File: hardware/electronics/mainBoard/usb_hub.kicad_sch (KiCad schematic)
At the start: 18 parts, among them J4 MUSBRM1C1M0, U4 USB2422-I/MJ

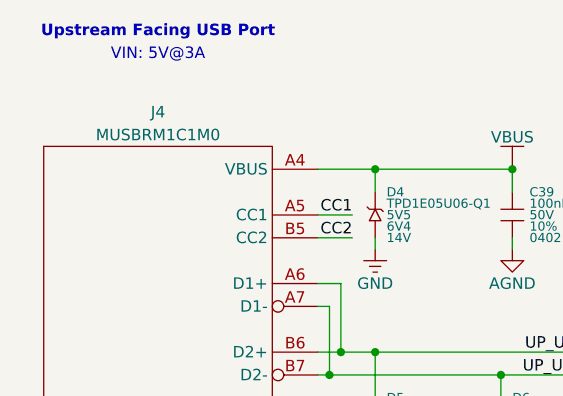
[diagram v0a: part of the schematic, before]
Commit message: renumber references
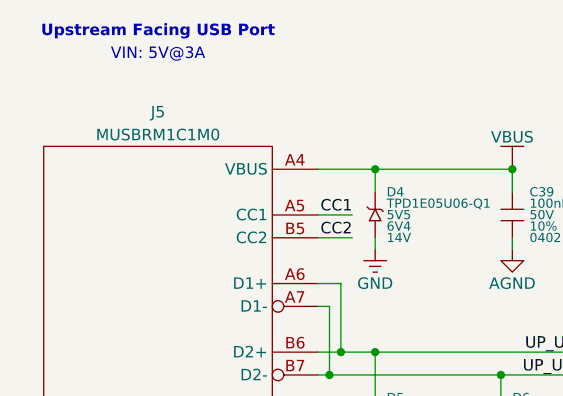
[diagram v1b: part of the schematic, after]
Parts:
- renumbered J4 to J5
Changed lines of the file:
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@@
 		(dnp no)
 		(fields_autoplaced yes)
-		(property "Reference" "#PWR091"
+		(property "Reference" "#PWR093"
 			(at 139.7 106.68 0)
 			(effects
@@
 			(project ""
 				(path "/be16e32f-2ccf-4272-9ec7-94d5fe7a55e0/6c7769dd-a66e-4549-9d6a-78682acf15fa"
-					(reference "#PWR091")
+					(reference "#PWR093")
 					(unit 1)
 				)
@@
 		(dnp no)
 		(fields_autoplaced yes)
-		(property "Reference" "#PWR0103"
+		(property "Reference" "#PWR0105"
 			(at 81.28 147.32 0)
 			(effects
@@
 			(project "mainBoard"
 				(path "/be16e32f-2ccf-4272-9ec7-94d5fe7a55e0/6c7769dd-a66e-4549-9d6a-78682acf15fa"
-					(reference "#PWR0103")
+					(reference "#PWR0105")
 					(unit 1)
 				)
@@
 		(dnp no)
 		(fields_autoplaced yes)
-		(property "Reference" "#PWR098"
+		(property "Reference" "#PWR0100"
 			(at 220.98 134.62 0)
 			(effects
@@
 			(project "mainBoard"
 				(path "/be16e32f-2ccf-4272-9ec7-94d5fe7a55e0/6c7769dd-a66e-4549-9d6a-78682acf15fa"
-					(reference "#PWR098")
+					(reference "#PWR0100")
 					(unit 1)
 				)
@@
 		(dnp no)
 		(fields_autoplaced yes)
-		(property "Reference" "#PWR086"
+		(property "Reference" "#PWR088"
 			(at 115.57 77.47 0)
 			(effects
@@
 			(project "mainBoard"
 				(path "/be16e32f-2ccf-4272-9ec7-94d5fe7a55e0/6c7769dd-a66e-4549-9d6a-78682acf15fa"
-					(reference "#PWR086")
+					(reference "#PWR088")
 					(unit 1)
 				)
@@
 		(dnp no)
 		(fields_autoplaced yes)
-		(property "Reference" "#PWR089"
+		(property "Reference" "#PWR091"
 			(at 115.57 86.36 0)
 			(effects
@@
 			(project "mainBoard"
 				(path "/be16e32f-2ccf-4272-9ec7-94d5fe7a55e0/6c7769dd-a66e-4549-9d6a-78682acf15fa"
-					(reference "#PWR089")
+					(reference "#PWR091")
 					(unit 1)
 				)
@@
 		(dnp no)
 		(fields_autoplaced yes)
-		(property "Reference" "#PWR088"
+		(property "Reference" "#PWR090"
 			(at 100.33 86.36 0)
 			(effects
@@
 			(project "mainBoard"
 				(path "/be16e32f-2ccf-4272-9ec7-94d5fe7a55e0/6c7769dd-a66e-4549-9d6a-78682acf15fa"
-					(reference "#PWR088")
+					(reference "#PWR090")
 					(unit 1)
 				)
@@
 		(dnp no)
 		(fields_autoplaced yes)
-		(property "Reference" "#PWR092"
+		(property "Reference" "#PWR094"
 			(at 152.4 106.68 0)
 			(effects
@@
 			(project "mainBoard"
 				(path "/be16e32f-2ccf-4272-9ec7-94d5fe7a55e0/6c7769dd-a66e-4549-9d6a-78682acf15fa"
-					(reference "#PWR092")
+					(reference "#PWR094")
 					(unit 1)
 				)
@@
 		(dnp no)
 		(fields_autoplaced yes)
-		(property "Reference" "#PWR0102"
+		(property "Reference" "#PWR0104"
 			(at 76.2 147.32 0)
 			(effects
@@
 			(project "mainBoard"
 				(path "/be16e32f-2ccf-4272-9ec7-94d5fe7a55e0/6c7769dd-a66e-4549-9d6a-78682acf15fa"
-					(reference "#PWR0102")
+					(reference "#PWR0104")
 					(unit 1)
 				)
@@
 		(dnp no)
 		(fields_autoplaced yes)
-		(property "Reference" "#PWR095"
+		(property "Reference" "#PWR097"
 			(at 146.05 113.03 0)
 			(effects
@@
 			(project "mainBoard"
 				(path "/be16e32f-2ccf-4272-9ec7-94d5fe7a55e0/6c7769dd-a66e-4549-9d6a-78682acf15fa"
-					(reference "#PWR095")
+					(reference "#PWR097")
 					(unit 1)
 				)
@@
 		(dnp no)
 		(fields_autoplaced yes)
-		(property "Reference" "#PWR093"
+		(property "Reference" "#PWR095"
 			(at 100.33 109.22 0)
 			(effects
@@
 			(project "mainBoard"
 				(path "/be16e32f-2ccf-4272-9ec7-94d5fe7a55e0/6c7769dd-a66e-4549-9d6a-78682acf15fa"
-					(reference "#PWR093")
+					(reference "#PWR095")
 					(unit 1)
 				)
@@
 		(dnp no)
 		(fields_autoplaced yes)
-		(property "Reference" "#PWR0101"
+		(property "Reference" "#PWR0103"
 			(at 71.12 147.32 0)
 			(effects
@@
 			(project "mainBoard"
 				(path "/be16e32f-2ccf-4272-9ec7-94d5fe7a55e0/6c7769dd-a66e-4549-9d6a-78682acf15fa"
-					(reference "#PWR0101")
+					(reference "#PWR0103")
 					(unit 1)
 				)
@@
 		(dnp no)
 		(fields_autoplaced yes)
-		(property "Reference" "J4"
+		(property "Reference" "J5"
 			(at 76.2 71.12 0)
 			(do_not_autoplace yes)
@@
 			(project "mainBoard"
 				(path "/be16e32f-2ccf-4272-9ec7-94d5fe7a55e0/6c7769dd-a66e-4549-9d6a-78682acf15fa"
-					(reference "J4")
+					(reference "J5")
 					(unit 1)
 				)
@@
 		(dnp no)
 		(fields_autoplaced yes)
-		(property "Reference" "#PWR096"
+		(property "Reference" "#PWR098"
 			(at 101.6 127 0)
 			(effects
@@
 			(project "mainBoard"
 				(path "/be16e32f-2ccf-4272-9ec7-94d5fe7a55e0/6c7769dd-a66e-4549-9d6a-78682acf15fa"
-					(reference "#PWR096")
+					(reference "#PWR098")
 					(unit 1)
 				)
@@
 		(dnp no)
 		(fields_autoplaced yes)
-		(property "Reference" "#PWR099"
+		(property "Reference" "#PWR0101"
 			(at 228.6 137.16 0)
 			(effects
@@
 			(project "mainBoard"
 				(path "/be16e32f-2ccf-4272-9ec7-94d5fe7a55e0/6c7769dd-a66e-4549-9d6a-78682acf15fa"
-					(reference "#PWR099")
+					(reference "#PWR0101")
 					(unit 1)
 				)
@@
 		(dnp no)
 		(fields_autoplaced yes)
-		(property "Reference" "#PWR087"
+		(property "Reference" "#PWR089"
 			(at 152.4 82.55 0)
 			(effects
@@
 			(project ""
 				(path "/be16e32f-2ccf-4272-9ec7-94d5fe7a55e0/6c7769dd-a66e-4549-9d6a-78682acf15fa"
-					(reference "#PWR087")
+					(reference "#PWR089")
 					(unit 1)
 				)
@@
 		(dnp no)
 		(fields_autoplaced yes)
-		(property "Reference" "#PWR085"
+		(property "Reference" "#PWR087"
 			(at 152.4 71.12 0)
 			(effects
@@
 			(project ""
 				(path "/be16e32f-2ccf-4272-9ec7-94d5fe7a55e0/6c7769dd-a66e-4549-9d6a-78682acf15fa"
-					(reference "#PWR085")
+					(reference "#PWR087")
 					(unit 1)
 				)
@@
 		(dnp no)
 		(fields_autoplaced yes)
-		(property "Reference" "#PWR090"
+		(property "Reference" "#PWR092"
 			(at 139.7 95.25 0)
 			(effects
@@
 			(project "mainBoard"
 				(path "/be16e32f-2ccf-4272-9ec7-94d5fe7a55e0/6c7769dd-a66e-4549-9d6a-78682acf15fa"
-					(reference "#PWR090")
+					(reference "#PWR092")
 					(unit 1)
 				)
@@
 		(dnp no)
 		(fields_autoplaced yes)
-		(property "Reference" "#PWR0100"
+		(property "Reference" "#PWR0102"
 			(at 241.3 137.16 0)
 			(effects
@@
 			(project "mainBoard"
 				(path "/be16e32f-2ccf-4272-9ec7-94d5fe7a55e0/6c7769dd-a66e-4549-9d6a-78682acf15fa"
-					(reference "#PWR0100")
+					(reference "#PWR0102")
 					(unit 1)
 				)
@@
 		(dnp no)
 		(fields_autoplaced yes)
-		(property "Reference" "#PWR097"
+		(property "Reference" "#PWR099"
 			(at 114.3 127 0)
 			(effects
@@
 			(project "mainBoard"
 				(path "/be16e32f-2ccf-4272-9ec7-94d5fe7a55e0/6c7769dd-a66e-4549-9d6a-78682acf15fa"
-					(reference "#PWR097")
+					(reference "#PWR099")
 					(unit 1)
 				)
@@
 		(dnp no)
 		(fields_autoplaced yes)
-		(property "Reference" "#PWR094"
+		(property "Reference" "#PWR096"
 			(at 114.3 109.22 0)
 			(effects
@@
 			(project "mainBoard"
 				(path "/be16e32f-2ccf-4272-9ec7-94d5fe7a55e0/6c7769dd-a66e-4549-9d6a-78682acf15fa"
-					(reference "#PWR094")
+					(reference "#PWR096")
 					(unit 1)
 				)

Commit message: page size
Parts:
- R21: DKPN 541-12.0KLDKR-ND -> 541-12.0KLCT-ND
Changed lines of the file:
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@@
 	(generator "eeschema")
 	(generator_version "9.0")
-	(paper "USLetter")
+	(paper "B")
 	(title_block
 		(title "USB Hub")
@@
 		(polyline
 			(pts
-				(xy 106.68 96.52) (xy 106.68 101.6) (xy 109.22 101.6) (xy 109.22 96.52)
+				(xy 234.95 93.98) (xy 234.95 88.9) (xy 237.49 88.9) (xy 237.49 93.98)
 			)
 			(stroke
@@
 		(polyline
 			(pts
-				(xy 234.95 93.98) (xy 234.95 88.9) (xy 237.49 88.9) (xy 237.49 93.98)
+				(xy 106.68 96.52) (xy 106.68 101.6) (xy 109.22 101.6) (xy 109.22 96.52)
 			)
 			(stroke
@@
 			)
 		)
-		(property "DKPN" "541-12.0KLDKR-ND"
+		(property "DKPN" "541-12.0KLCT-ND"
 			(at 228.6 133.35 0)
 			(effects

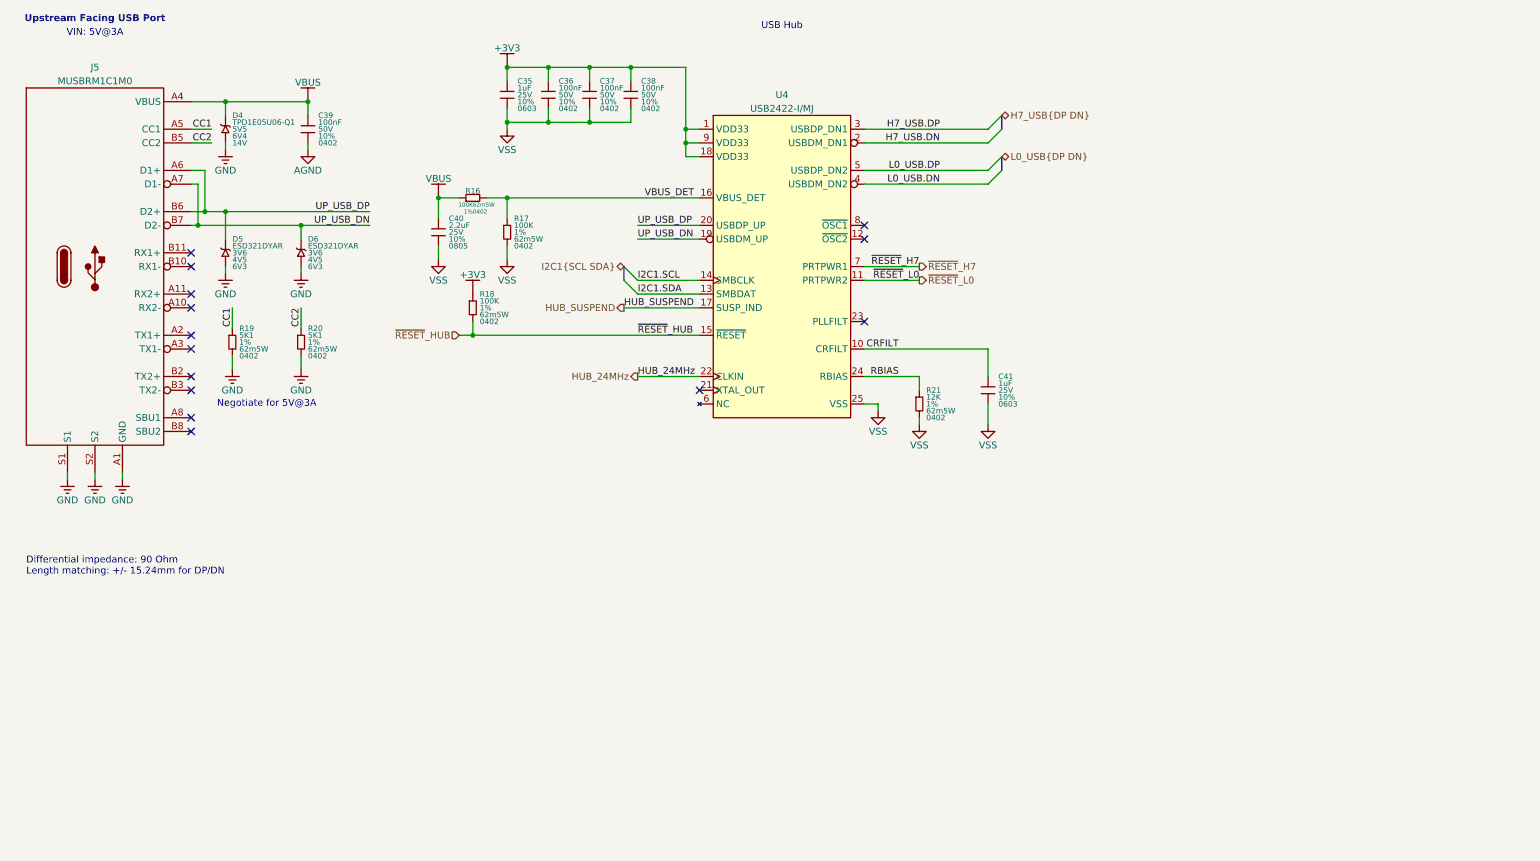
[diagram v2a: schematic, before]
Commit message: organized pages. added notes and net flags
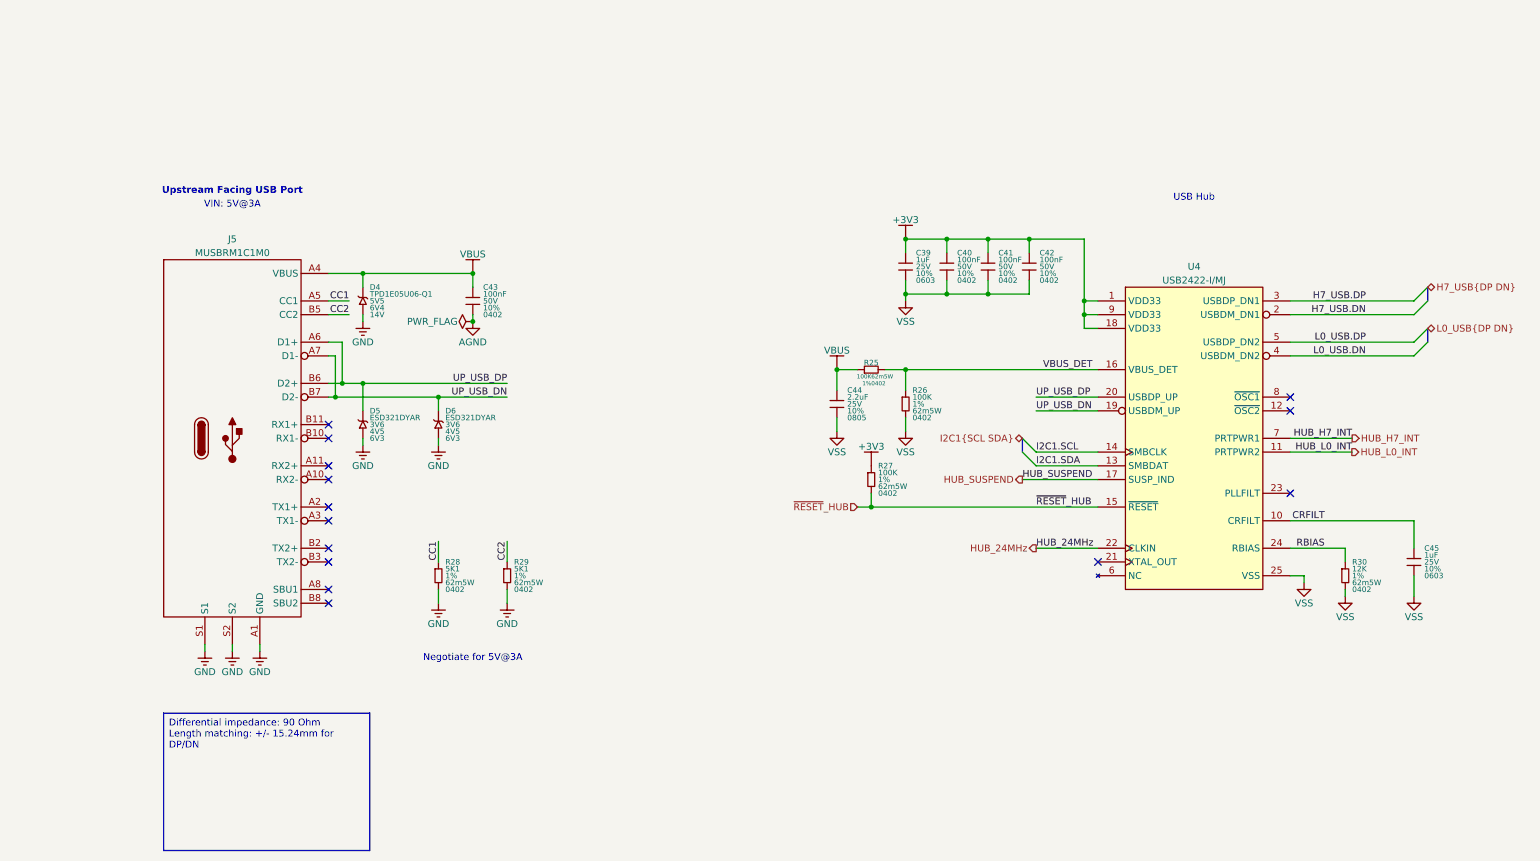
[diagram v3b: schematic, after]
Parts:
- renumbered C35 to C39, C36 to C40, C37 to C41, C38 to C42, C39 to C43, C40 to C44, C41 to C45, R16 to R25, R17 to R26, R18 to R27, R19 to R28, R20 to R29, R21 to R30
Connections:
- net ~{RESET}_H7 renamed HUB_H7_INT
- net ~{RESET}_L0 renamed HUB_L0_INT
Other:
- note removed: "Differential impedance: 90 Ohm Length matching: +/- 15.24mm for DP/DN"
- title: USB Hub -> Awohali USB Hub
- moved on the sheet: C39, C40, C41, C42, C43, C44, C45, D4, D5, D6, J5, R25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
